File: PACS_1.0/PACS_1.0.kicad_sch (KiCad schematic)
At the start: 8 parts, among them U1 MSP430G2553IN20

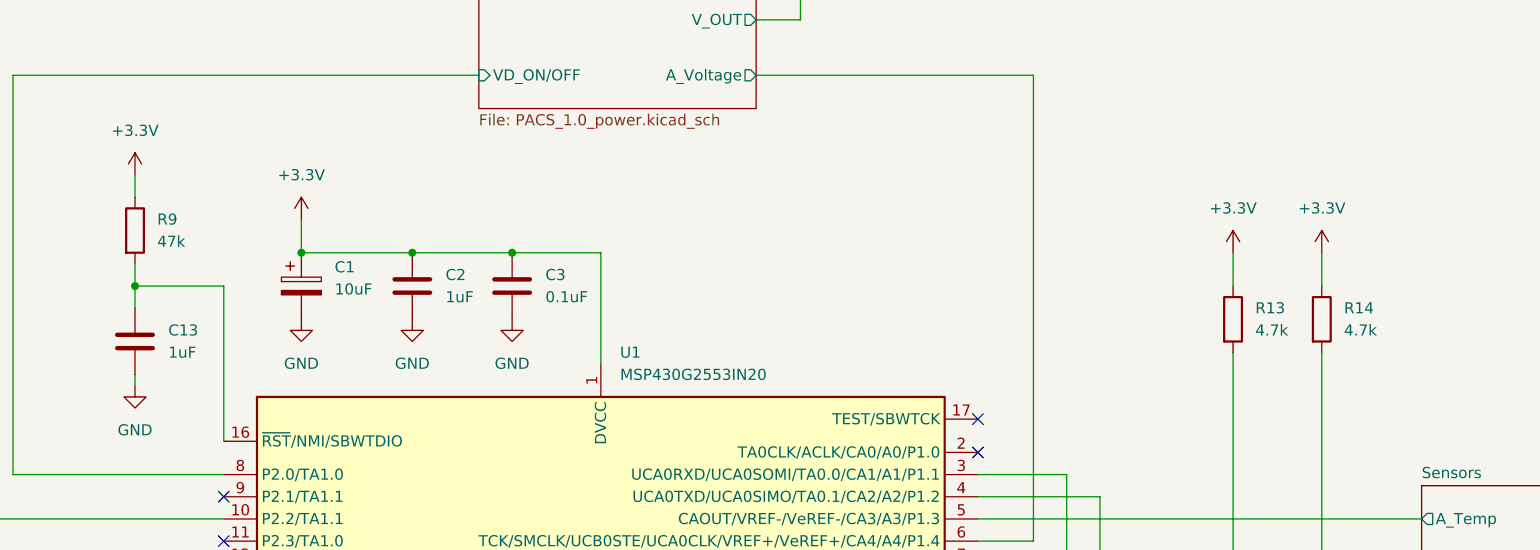
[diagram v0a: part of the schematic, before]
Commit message: Changed reference for Components
C8 to C2 (AS EXAMPLE)
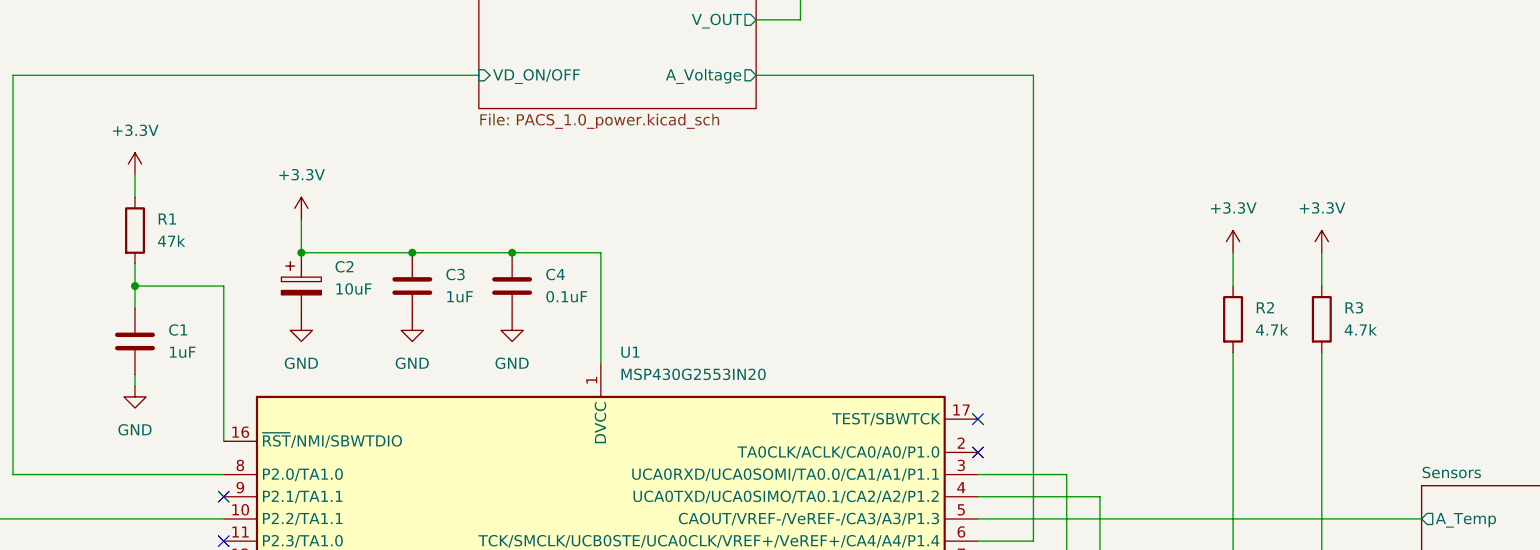
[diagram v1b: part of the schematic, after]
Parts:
- renumbered C13 to C1, C1 to C2, C2 to C3, C3 to C4, R9 to R1, R13 to R2, R14 to R3
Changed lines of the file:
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@@
 		(dnp no)
 		(fields_autoplaced yes)
-		(property "Reference" "C3"
+		(property "Reference" "C4"
 			(at 139.7 72.3899 0)
 			(effects
@@
 			(project ""
 				(path "/6996cbc8-fffb-40fd-8350-2bb7d19e6e7a"
-					(reference "C3")
+					(reference "C4")
 					(unit 1)
 				)
@@
 		(on_board yes)
 		(dnp no)
-		(property "Reference" "#PWR032"
+		(property "Reference" "#PWR01"
 			(at 92.71 64.77 0)
 			(effects
@@
 			(project "PACS_1.0"
 				(path "/6996cbc8-fffb-40fd-8350-2bb7d19e6e7a"
-					(reference "#PWR032")
+					(reference "#PWR01")
 					(unit 1)
 				)
@@
 		(dnp no)
 		(fields_autoplaced yes)
-		(property "Reference" "#PWR03"
+		(property "Reference" "#PWR05"
 			(at 124.46 83.82 0)
 			(effects
@@
 			(project "PACS_1.0"
 				(path "/6996cbc8-fffb-40fd-8350-2bb7d19e6e7a"
-					(reference "#PWR03")
+					(reference "#PWR05")
 					(unit 1)
 				)
@@
 		(dnp no)
 		(fields_autoplaced yes)
-		(property "Reference" "#PWR02"
+		(property "Reference" "#PWR06"
 			(at 135.89 83.82 0)
 			(effects
@@
 			(project "PACS_1.0"
 				(path "/6996cbc8-fffb-40fd-8350-2bb7d19e6e7a"
-					(reference "#PWR02")
+					(reference "#PWR06")
 					(unit 1)
 				)
@@
 		(dnp no)
 		(fields_autoplaced yes)
-		(property "Reference" "#PWR029"
+		(property "Reference" "#PWR010"
 			(at 228.6 73.66 0)
 			(effects
@@
 			(project "PACS_1.0"
 				(path "/6996cbc8-fffb-40fd-8350-2bb7d19e6e7a"
-					(reference "#PWR029")
+					(reference "#PWR010")
 					(unit 1)
 				)
@@
 		(dnp no)
 		(fields_autoplaced yes)
-		(property "Reference" "C13"
+		(property "Reference" "C1"
 			(at 96.52 78.7399 0)
 			(effects
@@
 			(project "PACS_1.0"
 				(path "/6996cbc8-fffb-40fd-8350-2bb7d19e6e7a"
-					(reference "C13")
+					(reference "C1")
 					(unit 1)
 				)
@@
 		(dnp no)
 		(fields_autoplaced yes)
-		(property "Reference" "#PWR028"
+		(property "Reference" "#PWR09"
 			(at 218.44 73.66 0)
 			(effects
@@
 			(project "PACS_1.0"
 				(path "/6996cbc8-fffb-40fd-8350-2bb7d19e6e7a"
-					(reference "#PWR028")
+					(reference "#PWR09")
 					(unit 1)
 				)
@@
 		(dnp no)
 		(fields_autoplaced yes)
-		(property "Reference" "R13"
+		(property "Reference" "R2"
 			(at 220.98 76.1999 0)
 			(effects
@@
 			(project "PACS_1.0"
 				(path "/6996cbc8-fffb-40fd-8350-2bb7d19e6e7a"
-					(reference "R13")
+					(reference "R2")
 					(unit 1)
 				)
@@
 		(dnp no)
 		(fields_autoplaced yes)
-		(property "Reference" "R14"
+		(property "Reference" "R3"
 			(at 231.14 76.1999 0)
 			(effects
@@
 			(project "PACS_1.0"
 				(path "/6996cbc8-fffb-40fd-8350-2bb7d19e6e7a"
-					(reference "R14")
+					(reference "R3")
 					(unit 1)
 				)
@@
 		(dnp no)
 		(fields_autoplaced yes)
-		(property "Reference" "C1"
+		(property "Reference" "C2"
 			(at 115.57 71.5009 0)
 			(effects
@@
 			(project ""
 				(path "/6996cbc8-fffb-40fd-8350-2bb7d19e6e7a"
-					(reference "C1")
+					(reference "C2")
 					(unit 1)
 				)
@@
 		(dnp no)
 		(fields_autoplaced yes)
-		(property "Reference" "#PWR010"
+		(property "Reference" "#PWR08"
 			(at 168.91 41.91 0)
 			(effects
@@
 			(project "PACS_1.0"
 				(path "/6996cbc8-fffb-40fd-8350-2bb7d19e6e7a"
-					(reference "#PWR010")
+					(reference "#PWR08")
 					(unit 1)
 				)
@@
 		(dnp no)
 		(fields_autoplaced yes)
-		(property "Reference" "#PWR033"
+		(property "Reference" "#PWR02"
 			(at 92.71 91.44 0)
 			(effects
@@
 			(project "PACS_1.0"
 				(path "/6996cbc8-fffb-40fd-8350-2bb7d19e6e7a"
-					(reference "#PWR033")
+					(reference "#PWR02")
 					(unit 1)
 				)
@@
 		(dnp no)
 		(fields_autoplaced yes)
-		(property "Reference" "C2"
+		(property "Reference" "C3"
 			(at 128.27 72.3899 0)
 			(effects
@@
 			(project ""
 				(path "/6996cbc8-fffb-40fd-8350-2bb7d19e6e7a"
-					(reference "C2")
+					(reference "C3")
 					(unit 1)
 				)
@@
 		(dnp no)
 		(fields_autoplaced yes)
-		(property "Reference" "#PWR05"
+		(property "Reference" "#PWR03"
 			(at 111.76 69.85 0)
 			(effects
@@
 			(project ""
 				(path "/6996cbc8-fffb-40fd-8350-2bb7d19e6e7a"
-					(reference "#PWR05")
+					(reference "#PWR03")
 					(unit 1)
 				)
@@
 		(dnp no)
 		(fields_autoplaced yes)
-		(property "Reference" "R9"
+		(property "Reference" "R1"
 			(at 95.25 66.0399 0)
 			(effects
@@
 			(project ""
 				(path "/6996cbc8-fffb-40fd-8350-2bb7d19e6e7a"
-					(reference "R9")
+					(reference "R1")
 					(unit 1)
 				)
@@
 		(dnp no)
 		(fields_autoplaced yes)
-		(property "Reference" "#PWR01"
+		(property "Reference" "#PWR07"
 			(at 146.05 128.27 0)
 			(effects
@@
 			(project ""
 				(path "/6996cbc8-fffb-40fd-8350-2bb7d19e6e7a"
-					(reference "#PWR01")
-					(unit 1)
-				)
+					(reference "#PWR07")
+					(unit 1)
+				)

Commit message: Updated footprints for caps and resistors
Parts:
- C1, C3: footprint (none) -> Capacitor_SMD:C_0603_1608Metric
- C2: footprint (none) -> Capacitor_SMD:C_0805_2012Metric
- C4: footprint (none) -> Capacitor_SMD:C_0402_1005Metric
- R1: footprint (none) -> Resistor_SMD:R_0603_1608Metric
- R2, R3: footprint (none) -> Resistor_SMD:R_0402_1005Metric
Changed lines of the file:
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@@
 			)
 		)
-		(property "Footprint" ""
+		(property "Footprint" "Capacitor_SMD:C_0402_1005Metric"
 			(at 136.8552 77.47 0)
 			(effects
@@
 			)
 		)
-		(property "Footprint" ""
+		(property "Footprint" "Capacitor_SMD:C_0603_1608Metric"
 			(at 93.6752 83.82 0)
 			(effects
@@
 			)
 		)
-		(property "Footprint" ""
+		(property "Footprint" "Resistor_SMD:R_0402_1005Metric"
 			(at 216.662 77.47 90)
 			(effects
@@
 			)
 		)
-		(property "Footprint" ""
+		(property "Footprint" "Resistor_SMD:R_0402_1005Metric"
 			(at 226.822 77.47 90)
 			(effects
@@
 			)
 		)
-		(property "Footprint" ""
+		(property "Footprint" "Capacitor_SMD:C_0805_2012Metric"
 			(at 112.7252 77.47 0)
 			(effects
@@
 			)
 		)
-		(property "Footprint" ""
+		(property "Footprint" "Capacitor_SMD:C_0603_1608Metric"
 			(at 125.4252 77.47 0)
 			(effects
@@
 			)
 		)
-		(property "Footprint" ""
+		(property "Footprint" "Resistor_SMD:R_0603_1608Metric"
 			(at 90.932 67.31 90)
 			(effects
